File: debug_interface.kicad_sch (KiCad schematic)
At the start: 12 parts, among them SW3 Button Switch SPST-No, SW4 Button Switch SPST-No

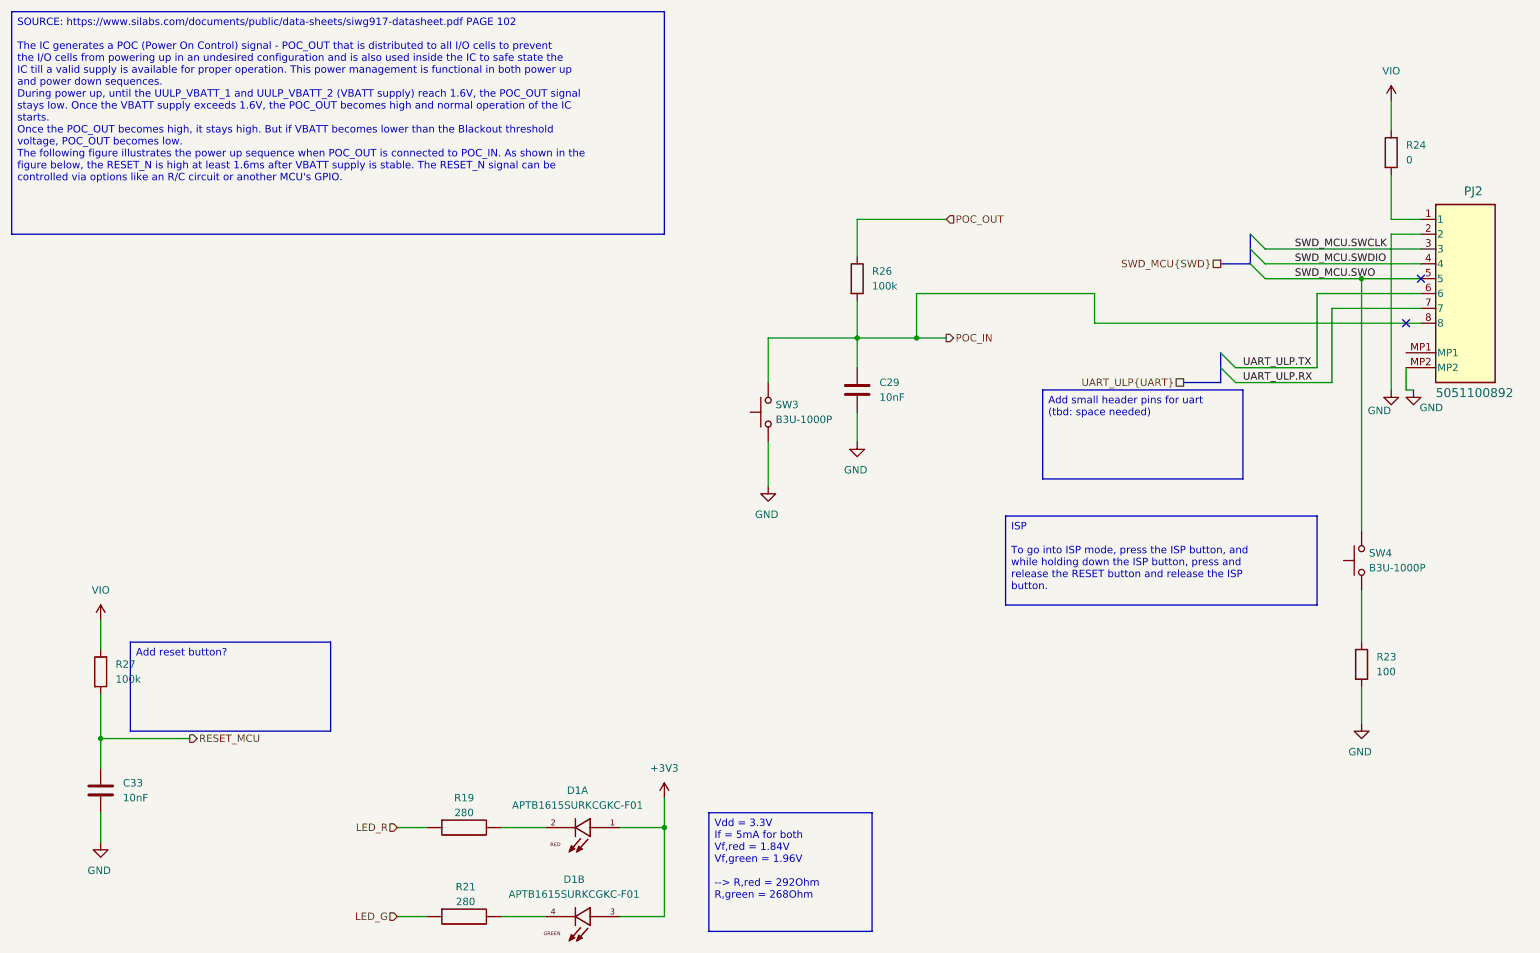
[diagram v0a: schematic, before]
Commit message: changes after first review: add lvl shifters, board at 1v8, new power tree
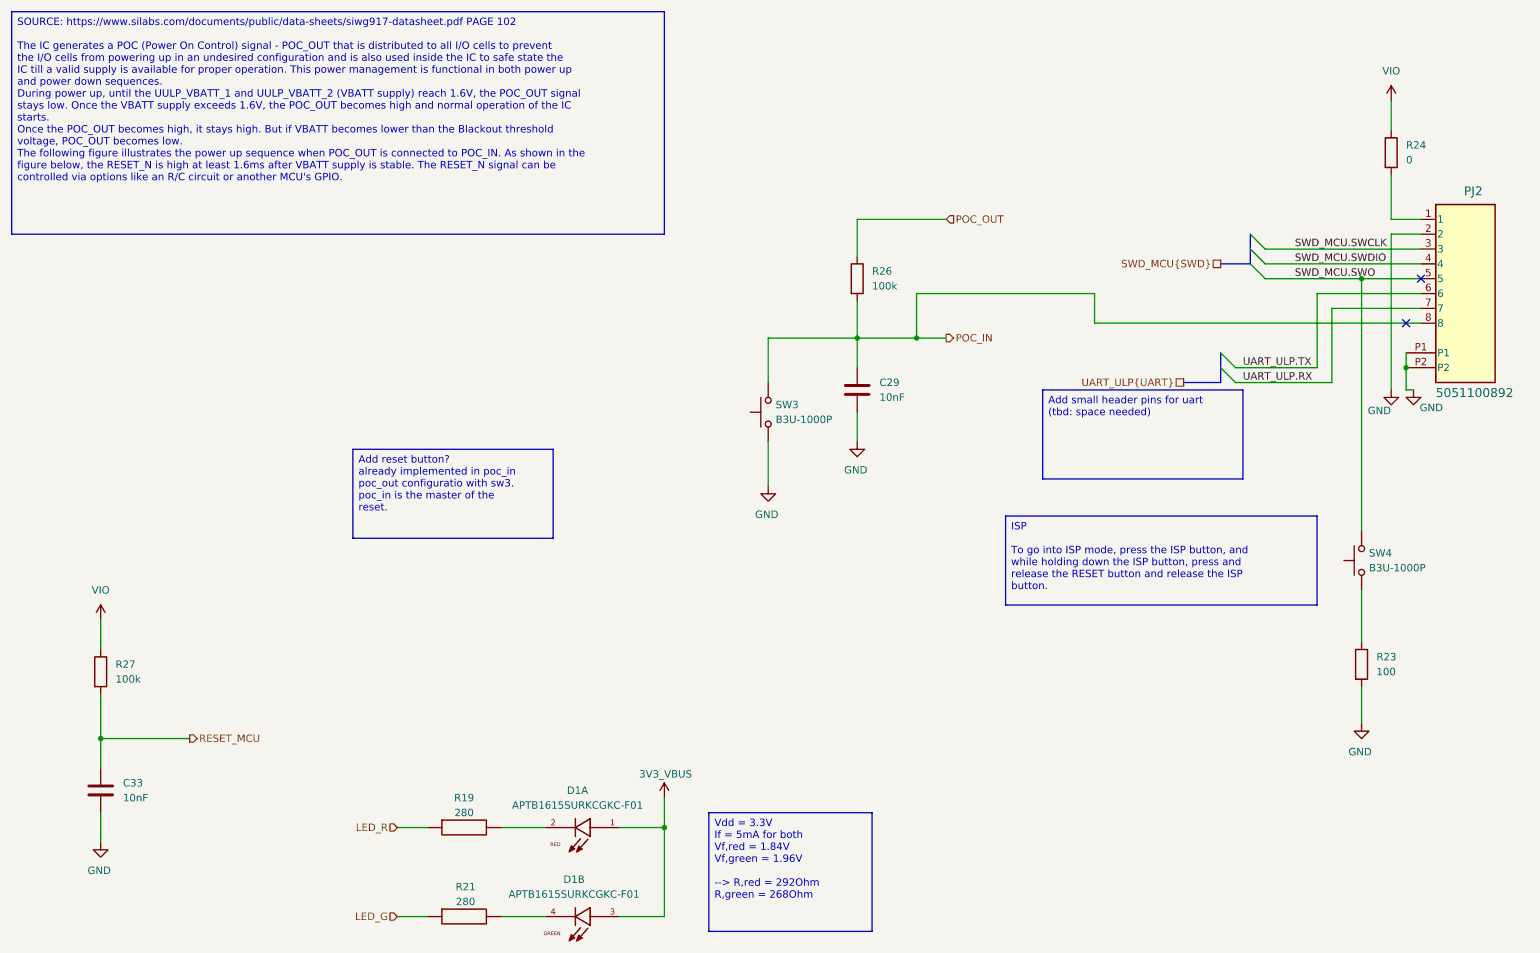
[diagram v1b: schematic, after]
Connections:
- net GND: now also PJ2.P1, PJ2.P2; no longer PJ2.MP2
- net +3V3 renamed 3V3_VBUS
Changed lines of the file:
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@@
 		)
 	)
-	(text_box "Add reset button? "
+	(text_box "Add reset button? \nalready implemented in poc_in poc_out configuratio with sw3. poc_in is the master of the reset."
 		(exclude_from_sim no)
-		(at 35.56 123.19 0)
+		(at 73.66 90.17 0)
 		(size 34.29 15.24)
 		(margins 0.9525 0.9525 0.9525 0.9525)
@@
 		(fill
 			(type color)
-			(color 255 153 0 1)
+			(color 253 255 49 1)
 		)
 		(effects
@@
 	)
 	(junction
+		(at 254 76.2)
+		(diameter 0)
+		(color 0 0 0 0)
+	)
+	(junction
 		(at 127 154.94)
 		(diameter 0)
@@
 	)
 	(no_connect
-		(at 256.54 60.96)
+		(at 254 68.58)
 	)
 	(no_connect
-		(at 254 68.58)
+		(at 256.54 60.96)
 	)
 	(bus_entry
@@
 	(wire
 		(pts
+			(xy 30.48 139.7) (xy 45.72 139.7)
+		)
+		(stroke
+			(width 0)
+			(type default)
+		)
+	)
+	(wire
+		(pts
 			(xy 99.06 170.18) (xy 106.68 170.18)
 		)
@@
 	(wire
 		(pts
+			(xy 254 73.66) (xy 254 76.2)
+		)
+		(stroke
+			(width 0)
+			(type default)
+		)
+	)
+	(wire
+		(pts
 			(xy 229.87 58.42) (xy 256.54 58.42)
 		)
@@
 	(wire
 		(pts
-			(xy 30.48 139.7) (xy 45.72 139.7)
-		)
-		(stroke
-			(width 0)
-			(type default)
-		)
-	)
-	(wire
-		(pts
 			(xy 241.3 78.74) (xy 241.3 66.04)
 		)
@@
 	)
 	(symbol
+		(lib_id "power:+BATT")
+		(at 127 149.86 0)
+		(unit 1)
+		(body_style 1)
+		(exclude_from_sim no)
+		(in_bom yes)
+		(on_board yes)
+		(in_pos_files yes)
+		(dnp no)
+		(property "Reference" "#PWR0114"
+			(at 127 153.67 0)
+			(hide yes)
+			(show_name no)
+			(do_not_autoplace no)
+			(effects
+				(font
+					(size 1.27 1.27)
+				)
+			)
+		)
+		(property "Value" "3V3_VBUS"
+			(at 122.682 145.796 0)
+			(show_name no)
+			(do_not_autoplace no)
+			(effects
+				(font
+					(size 1.27 1.27)
+				)
+				(justify left)
+			)
+		)
+		(property "Footprint" ""
+			(at 127 149.86 0)
+			(hide yes)
+			(show_name no)
+			(do_not_autoplace no)
+			(effects
+				(font
+					(size 1.27 1.27)
+				)
+			)
+		)
+		(property "Datasheet" ""
+			(at 127 149.86 0)
+			(hide yes)
+			(show_name no)
+			(do_not_autoplace no)
+			(effects
+				(font
+					(size 1.27 1.27)
+				)
+			)
+		)
+		(property "Description" "Power symbol creates a global label with name \"+BATT\""
+			(at 127 149.86 0)
+			(hide yes)
+			(show_name no)
+			(do_not_autoplace no)
+			(effects
+				(font
+					(size 1.27 1.27)
+				)
+			)
+		)
+		(pin "1"
+		)
+		(instances
+			(project "wius_new"
+				(path "/8543d6cf-82a6-4fc5-8760-a0773a1d6e4c/18cf3453-7c60-4f39-a40f-2a724a0c7370"
+					(reference "#PWR0114")
+					(unit 1)
+				)
+			)
+		)
+	)
+	(symbol
 		(lib_id "#dzdb:g_res/R-280-0402")
 		(at 83.82 170.18 0)
@@
 	)
 	(symbol
-		(lib_id "power:+3V3")
-		(at 127 149.86 0)
-		(unit 1)
-		(body_style 1)
-		(exclude_from_sim no)
-		(in_bom yes)
-		(on_board yes)
-		(in_pos_files yes)
-		(dnp no)
-		(fields_autoplaced yes)
-		(property "Reference" "#PWR055"
-			(at 127 153.67 0)
-			(hide yes)
-			(show_name no)
-			(do_not_autoplace no)
-			(effects
-				(font
-					(size 1.27 1.27)
-				)
-			)
-		)
-		(property "Value" "+3V3"
-			(at 127 144.78 0)
-			(show_name no)
-			(do_not_autoplace no)
-			(effects
-				(font
-					(size 1.27 1.27)
-				)
-			)
-		)
-		(property "Footprint" ""
-			(at 127 149.86 0)
-			(hide yes)
-			(show_name no)
-			(do_not_autoplace no)
-			(effects
-				(font
-					(size 1.27 1.27)
-				)
-			)
-		)
-		(property "Datasheet" ""
-			(at 127 149.86 0)
-			(hide yes)
-			(show_name no)
-			(do_not_autoplace no)
-			(effects
-				(font
-					(size 1.27 1.27)
-				)
-			)
-		)
-		(property "Description" "Power symbol creates a global label with name \"+3V3\""
-			(at 127 149.86 0)
-			(hide yes)
-			(show_name no)
-			(do_not_autoplace no)
-			(effects
-				(font
-					(size 1.27 1.27)
-				)
-			)
-		)
-		(pin "1"
-		)
-		(instances
-			(project "wius_new"
-				(path "/8543d6cf-82a6-4fc5-8760-a0773a1d6e4c/18cf3453-7c60-4f39-a40f-2a724a0c7370"
-					(reference "#PWR055")
-					(unit 1)
-				)
-			)
-		)
-	)
-	(symbol
 		(lib_id "power:GND")
 		(at 160.02 88.9 0)
@@
 		(pin "5"
 		)
-		(pin "MP1"
+		(pin "P2"
 		)
-		(pin "MP2"
+		(pin "P1"
 		)
 		(pin "7"
